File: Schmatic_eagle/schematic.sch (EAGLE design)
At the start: 2 parts, among them IC1 MEGA16-M

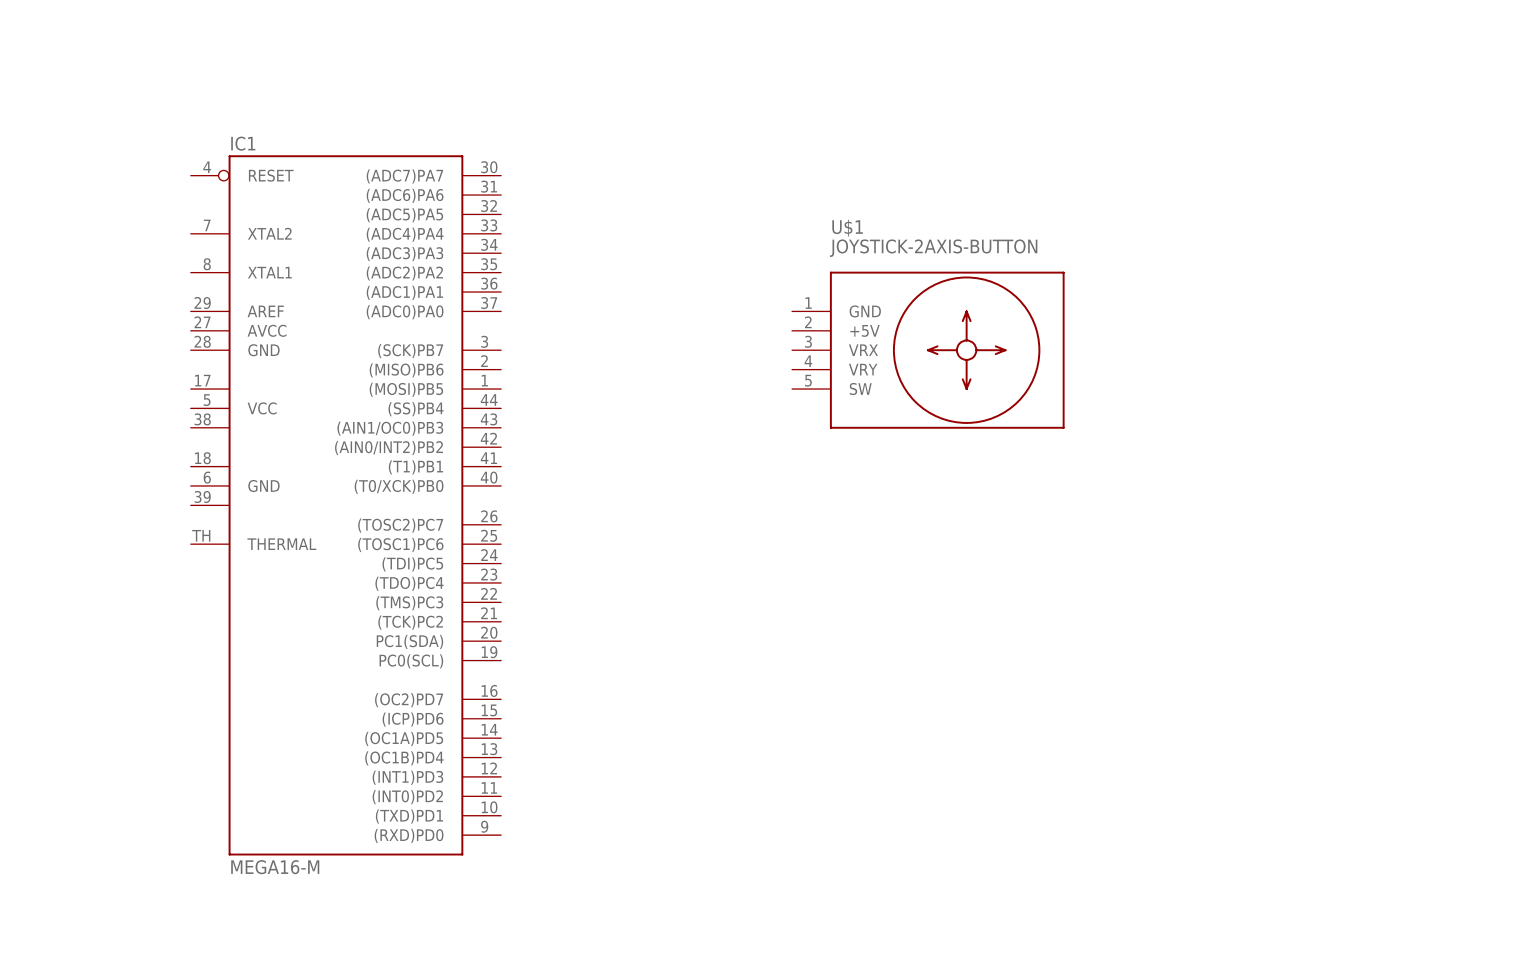
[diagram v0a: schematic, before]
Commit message: Schematic updates
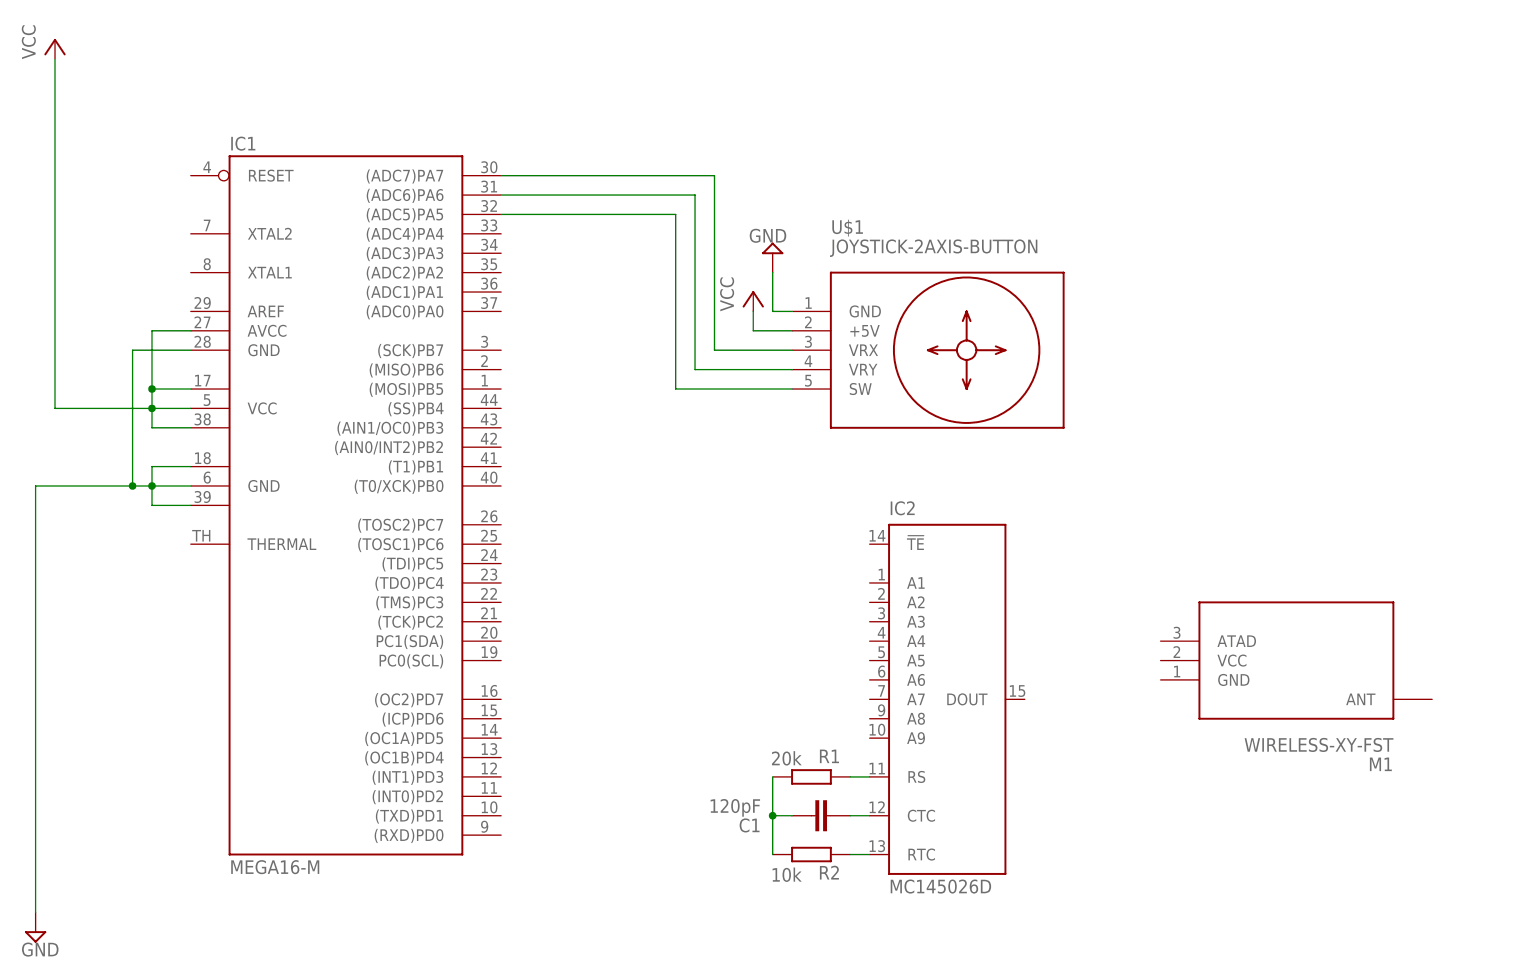
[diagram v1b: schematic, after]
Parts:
- added C1: 120pF, capacitor-wima:C2,5-3
- added IC2: MC145026D, micro-motorola:MC145026D
- added M1: WIRELESS-XY-FST, diy-modules:WIRELESS-XY-FST
- added R1: 20k, rcl:R-EU_01005
- added R2: 10k, rcl:R-EU_01005
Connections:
- new net GND: IC1.GND, IC1.GND1, IC1.GND2, IC1.GND@1, U$1.GND
- new net N$1: IC1.(ADC7)PA7, U$1.VRX
- new net N$2: IC1.(ADC6)PA6, U$1.VRY
- new net N$3: IC1.(ADC5)PA5, U$1.SW
- new net N$4: IC2G$1.RS, R1.1
- new net N$5: C1.2, IC2G$1.CTC
- new net N$6: IC2G$1.RTC, R2.1
- new net N$7: C1.1, R1.2, R2.2
- new net VCC: IC1.AVCC, IC1.VCC, IC1.VCC1, IC1.VCC2, U$1.+5V
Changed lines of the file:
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@@
 <part name="IC1" library="atmel" library_urn="urn:adsk.eagle:library:105" deviceset="MEGA16-M" device="" package3d_urn="urn:adsk.eagle:package:4352/1"/>
 <part name="U$1" library="diy-modules" deviceset="JOYSTICK-2AXIS-BUTTON" device=""/>
+<part name="SUPPLY2" library="supply2" library_urn="urn:adsk.eagle:library:372" deviceset="GND" device=""/>
+<part name="P+1" library="supply1" library_urn="urn:adsk.eagle:library:371" deviceset="VCC" device=""/>
+<part name="P+2" library="supply1" library_urn="urn:adsk.eagle:library:371" deviceset="VCC" device=""/>
+<part name="SUPPLY1" library="supply2" library_urn="urn:adsk.eagle:library:372" deviceset="GND" device=""/>
+<part name="M1" library="diy-modules" deviceset="WIRELESS-XY-FST" device=""/>
+<part name="IC2" library="micro-motorola" library_urn="urn:adsk.eagle:library:289" deviceset="MC145026" device="D" package3d_urn="urn:adsk.eagle:package:19964/1"/>
+<part name="C1" library="capacitor-wima" library_urn="urn:adsk.eagle:library:116" deviceset="C" device="2,5-3" package3d_urn="urn:adsk.eagle:package:5436/1" value="120pF"/>
+<part name="R1" library="rcl" library_urn="urn:adsk.eagle:library:334" deviceset="R-EU_" device="01005" package3d_urn="urn:adsk.eagle:package:26133/2" value="20k"/>
+<part name="R2" library="rcl" library_urn="urn:adsk.eagle:library:334" deviceset="R-EU_" device="01005" package3d_urn="urn:adsk.eagle:package:26133/2" value="10k"/>
 </parts>
 <sheets>
@@
 <attribute name="VALUE" x="228.6" y="147.32" size="1.778" layer="96"/>
 </instance>
+<instance part="SUPPLY2" gate="GND" x="220.98" y="147.32" smashed="yes" rot="R180">
+<attribute name="VALUE" x="222.885" y="150.495" size="1.778" layer="96" rot="R180"/>
+</instance>
+<instance part="P+1" gate="VCC" x="218.44" y="142.24" smashed="yes">
+<attribute name="VALUE" x="215.9" y="139.7" size="1.778" layer="96" rot="R90"/>
+</instance>
+<instance part="P+2" gate="VCC" x="127" y="175.26" smashed="yes">
+<attribute name="VALUE" x="124.46" y="172.72" size="1.778" layer="96" rot="R90"/>
+</instance>
+<instance part="SUPPLY1" gate="GND" x="124.46" y="58.42" smashed="yes">
+<attribute name="VALUE" x="122.555" y="55.245" size="1.778" layer="96"/>
+</instance>
+<instance part="M1" gate="G$1" x="289.56" y="93.98" smashed="yes" rot="R180">
+<attribute name="NAME" x="302.26" y="81.28" size="1.778" layer="95" rot="R180"/>
+<attribute name="VALUE" x="302.26" y="83.82" size="1.778" layer="96" rot="R180"/>
+</instance>
+<instance part="IC2" gate="G$1" x="243.84" y="88.9" smashed="yes">
+<attribute name="NAME" x="236.22" y="113.03" size="1.778" layer="95"/>
+<attribute name="VALUE" x="236.22" y="63.5" size="1.778" layer="96"/>
+</instance>
+<instance part="C1" gate="G$1" x="226.06" y="73.66" smashed="yes" rot="R90">
+<attribute name="NAME" x="219.456" y="73.279" size="1.778" layer="95" rot="R180"/>
+<attribute name="VALUE" x="219.456" y="75.819" size="1.778" layer="96" rot="R180"/>
+</instance>
+<instance part="R1" gate="G$1" x="226.06" y="78.74" smashed="yes" rot="R180">
+<attribute name="NAME" x="229.87" y="82.3214" size="1.778" layer="95" rot="R180"/>
+<attribute name="VALUE" x="224.79" y="82.042" size="1.778" layer="96" rot="R180"/>
+</instance>
+<instance part="R2" gate="G$1" x="226.06" y="68.58" smashed="yes" rot="R180">
+<attribute name="NAME" x="229.87" y="67.0814" size="1.778" layer="95" rot="R180"/>
+<attribute name="VALUE" x="224.79" y="66.802" size="1.778" layer="96" rot="R180"/>
+</instance>
 </instances>
 <busses>
 </busses>
 <nets>
+<net name="N$1" class="0">
+<segment>
+<pinref part="U$1" gate="G$1" pin="VRX"/>
+<wire x1="223.52" y1="134.62" x2="213.36" y2="134.62" width="0.1524" layer="91"/>
+<wire x1="213.36" y1="134.62" x2="213.36" y2="157.48" width="0.1524" layer="91"/>
+<pinref part="IC1" gate="G$1" pin="(ADC7)PA7"/>
+<wire x1="213.36" y1="157.48" x2="185.42" y2="157.48" width="0.1524" layer="91"/>
+</segment>
+</net>
+<net name="N$2" class="0">
+<segment>
+<pinref part="U$1" gate="G$1" pin="VRY"/>
+<wire x1="223.52" y1="132.08" x2="210.82" y2="132.08" width="0.1524" layer="91"/>
+<wire x1="210.82" y1="132.08" x2="210.82" y2="154.94" width="0.1524" layer="91"/>
+<pinref part="IC1" gate="G$1" pin="(ADC6)PA6"/>
+<wire x1="210.82" y1="154.94" x2="185.42" y2="154.94" width="0.1524" layer="91"/>
+</segment>
+</net>
+<net name="N$3" class="0">
+<segment>
+<pinref part="IC1" gate="G$1" pin="(ADC5)PA5"/>
+<wire x1="185.42" y1="152.4" x2="208.28" y2="152.4" width="0.1524" layer="91"/>
+<wire x1="208.28" y1="152.4" x2="208.28" y2="129.54" width="0.1524" layer="91"/>
+<pinref part="U$1" gate="G$1" pin="SW"/>
+<wire x1="208.28" y1="129.54" x2="223.52" y2="129.54" width="0.1524" layer="91"/>
+</segment>
+</net>
+<net name="VCC" class="0">
+<segment>
+<pinref part="U$1" gate="G$1" pin="+5V"/>
+<wire x1="223.52" y1="137.16" x2="218.44" y2="137.16" width="0.1524" layer="91"/>
+<pinref part="P+1" gate="VCC" pin="VCC"/>
+<wire x1="218.44" y1="137.16" x2="218.44" y2="139.7" width="0.1524" layer="91"/>
+</segment>
+<segment>
+<pinref part="P+2" gate="VCC" pin="VCC"/>
+<wire x1="127" y1="172.72" x2="127" y2="127" width="0.1524" layer="91"/>
+<pinref part="IC1" gate="G$1" pin="VCC"/>
+<wire x1="127" y1="127" x2="139.7" y2="127" width="0.1524" layer="91"/>
+<junction x="139.7" y="127"/>
+<wire x1="139.7" y1="127" x2="144.78" y2="127" width="0.1524" layer="91"/>
+<pinref part="IC1" gate="G$1" pin="VCC1"/>
+<wire x1="144.78" y1="129.54" x2="139.7" y2="129.54" width="0.1524" layer="91"/>
+<wire x1="139.7" y1="129.54" x2="139.7" y2="127" width="0.1524" layer="91"/>
+<pinref part="IC1" gate="G$1" pin="VCC2"/>
+<wire x1="144.78" y1="124.46" x2="139.7" y2="124.46" width="0.1524" layer="91"/>
+<wire x1="139.7" y1="124.46" x2="139.7" y2="127" width="0.1524" layer="91"/>
+<pinref part="IC1" gate="G$1" pin="AVCC"/>
+<wire x1="144.78" y1="137.16" x2="139.7" y2="137.16" width="0.1524" layer="91"/>
+<wire x1="139.7" y1="137.16" x2="139.7" y2="129.54" width="0.1524" layer="91"/>
+<junction x="139.7" y="129.54"/>
+</segment>
+</net>
+<net name="GND" class="0">
+<segment>
+<pinref part="SUPPLY2" gate="GND" pin="GND"/>
+<pinref part="U$1" gate="G$1" pin="GND"/>
+<wire x1="220.98" y1="144.78" x2="220.98" y2="139.7" width="0.1524" layer="91"/>
+<wire x1="220.98" y1="139.7" x2="223.52" y2="139.7" width="0.1524" layer="91"/>
+</segment>
+<segment>
+<pinref part="SUPPLY1" gate="GND" pin="GND"/>
+<pinref part="IC1" gate="G$1" pin="GND"/>
+<wire x1="124.46" y1="60.96" x2="124.46" y2="116.84" width="0.1524" layer="91"/>
+<wire x1="124.46" y1="116.84" x2="137.16" y2="116.84" width="0.1524" layer="91"/>
+<junction x="139.7" y="116.84"/>
+<wire x1="137.16" y1="116.84" x2="139.7" y2="116.84" width="0.1524" layer="91"/>
+<wire x1="139.7" y1="116.84" x2="144.78" y2="116.84" width="0.1524" layer="91"/>
+<pinref part="IC1" gate="G$1" pin="GND1"/>
+<wire x1="144.78" y1="119.38" x2="139.7" y2="119.38" width="0.1524" layer="91"/>
+<wire x1="139.7" y1="119.38" x2="139.7" y2="116.84" width="0.1524" layer="91"/>
+<pinref part="IC1" gate="G$1" pin="GND2"/>
+<wire x1="144.78" y1="114.3" x2="139.7" y2="114.3" width="0.1524" layer="91"/>
+<wire x1="139.7" y1="114.3" x2="139.7" y2="116.84" width="0.1524" layer="91"/>
+<pinref part="IC1" gate="G$1" pin="GND@1"/>
+<wire x1="144.78" y1="134.62" x2="137.16" y2="134.62" width="0.1524" layer="91"/>
+<wire x1="137.16" y1="134.62" x2="137.16" y2="116.84" width="0.1524" layer="91"/>
+<junction x="137.16" y="116.84"/>
+</segment>
+</net>
+<net name="N$4" class="0">
+<segment>
+<pinref part="R1" gate="G$1" pin="1"/>
+<pinref part="IC2" gate="G$1" pin="RS"/>
+<wire x1="231.14" y1="78.74" x2="233.68" y2="78.74" width="0.1524" layer="91"/>
+</segment>
+</net>
+<net name="N$5" class="0">
+<segment>
+<pinref part="IC2" gate="G$1" pin="CTC"/>
+<pinref part="C1" gate="G$1" pin="2"/>
+<wire x1="233.68" y1="73.66" x2="231.14" y2="73.66" width="0.1524" layer="91"/>
+</segment>
+</net>
+<net name="N$6" class="0">
+<segment>
+<pinref part="R2" gate="G$1" pin="1"/>
+<pinref part="IC2" gate="G$1" pin="RTC"/>
+<wire x1="231.14" y1="68.58" x2="233.68" y2="68.58" width="0.1524" layer="91"/>
+</segment>
+</net>
+<net name="N$7" class="0">
+<segment>
+<pinref part="R1" gate="G$1" pin="2"/>
+<pinref part="R2" gate="G$1" pin="2"/>
+<wire x1="220.98" y1="78.74" x2="220.98" y2="73.66" width="0.1524" layer="91"/>
+<pinref part="C1" gate="G$1" pin="1"/>
+<wire x1="220.98" y1="73.66" x2="220.98" y2="68.58" width="0.1524" layer="91"/>
+<wire x1="223.52" y1="73.66" x2="220.98" y2="73.66" width="0.1524" layer="91"/>
+<junction x="220.98" y="73.66"/>
+</segment>
+</net>
 </nets>
 </sheet>
@@
 packages will not be understood (or retained) with this version.
 </note>
+<note version="8.4" severity="warning">
+Since Version 8.4, EAGLE supports properties for SPICE simulation.
+Probes in schematics and SPICE mapping objects found in parts and library devices
+will not be understood with this version. Update EAGLE to the latest version
+for full support of SPICE simulation.
+</note>
 </compatibility>
